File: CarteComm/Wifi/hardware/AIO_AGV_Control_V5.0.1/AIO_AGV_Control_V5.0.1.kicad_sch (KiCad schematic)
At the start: 57 parts, among them J1 DB25_Pins, J2 DB25_Socket, T1 IRF520, T10 IRF520, T11 IRF520, T12 IRF520, T14 IRF520, T15 IRF520, T16 IRF520, T17 IRF520, T18 IRF520, T19 IRF520, T2 IRF520, T20 IRF520, T21 IRF520, T22 IRF520, T23 IRF520, T24 IRF520, T3 IRF520, T4 IRF520, T5 IRF520, T6 IRF520, T7 IRF520, T8 IRF520, T9 IRF520, U1 ESP32-DEVKITC

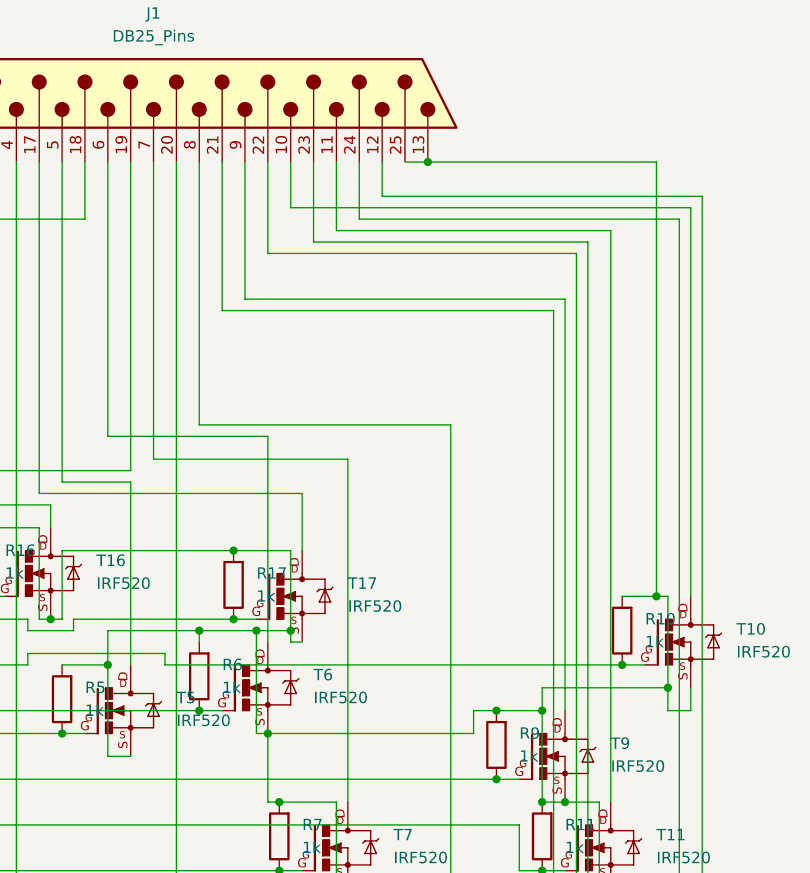
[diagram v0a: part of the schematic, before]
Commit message: test(lora): essais radio d'émission et de réception, côté ESP32 et côté Linux
Deux sous-dossiers dans LoRa/test/, chacun avec un essai d'émission et un de
réception, donc quatre combinaisons possibles. Les deux croisées - ESP32 vers
Linux et Linux vers ESP32 - sont les seules qui prouvent quelque chose : une
implémentation confrontée à elle-même ne démontre que sa propre cohérence.

Le point de conception est là. Une radio qui porte et des trames qui divergent
d'un bit donnent un banc parfait et une panne en atelier, alors les deux côtés
parlent la trame applicative du projet, pas un message d'essai. Côté ESP32 les
sketches compilent le pilote Sx1276Radio et le DutyCycleBudget du dépôt ; côté
Linux, agv_frame.py est un portage fidèle de frame.cpp.

Ce portage n'est pas pris sur parole : test_interop_trame.py compile le codec
C++ du coeur, lui fait produire des vecteurs et compare octet à octet. Six
vecteurs, extension d'horodatage comprise, zéro écart. C'est le seul essai du
dossier qui tourne sans matériel.

Le budget de rapport cyclique est appliqué des deux côtés, accusés compris - un
récepteur qui acquitte est un émetteur. Les deux essais de réception alertent
sous -115 dBm de RSSI : un lien qui passe tout juste ne passe pas une fois un
chariot chargé entre les antennes.

Le brochage ESP32 par défaut reprend les broches relevées libres au KiCad, avec
un static_assert contre IO16 et IO17 qui portent la liaison vers le MEGA.

Le README rappelle qu'un Gate G100 ne peut pas faire tourner les scripts unipi :
boîtier fermé, ni SPI ni GPIO.

Co-Authored-By: Claude Opus 5 <noreply@anthropic.com>
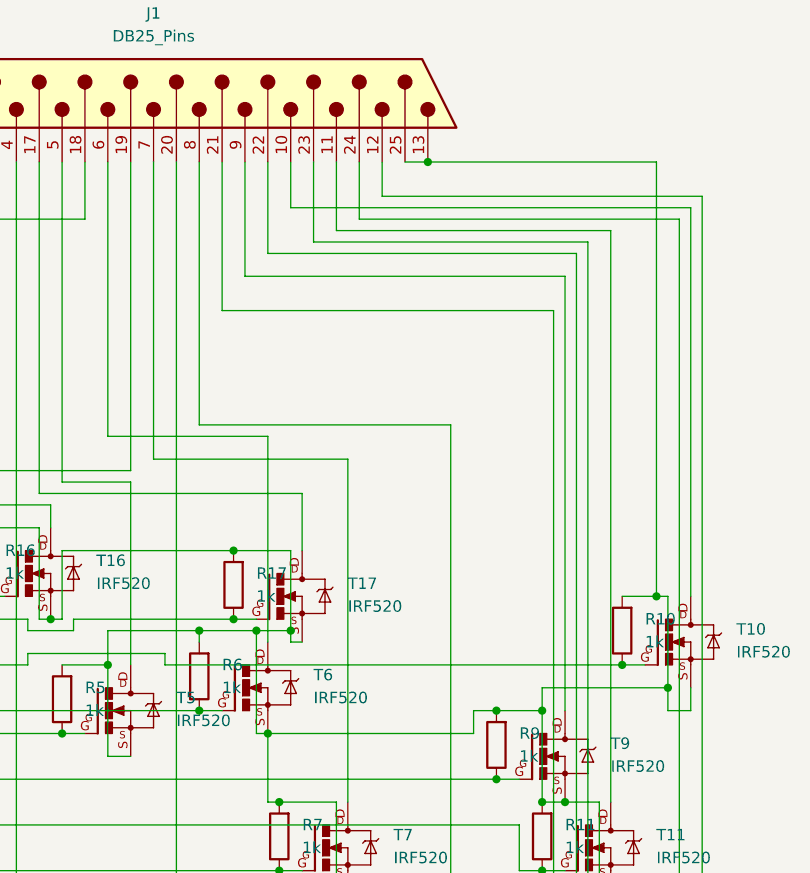
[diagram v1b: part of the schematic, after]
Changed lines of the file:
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@@
-	(wire
-		(pts
-			(xy 266.7 43.18) (xy 266.7 88.9)
-		)
-		(stroke
-			(width 0)
-			(type default)
-		)
-	)
 	(wire
 		(pts
@@
 	(wire
 		(pts
-			(xy 231.14 27.94) (xy 231.14 43.18)
+			(xy 231.14 27.94) (xy 231.14 40.64)
 		)
 		(stroke
@@
 	(wire
 		(pts
-			(xy 231.14 43.18) (xy 266.7 43.18)
+			(xy 231.14 40.64) (xy 266.7 40.64)
 		)
 		(stroke
@@
 		)
 		(stroke
+			(width 0)
+			(type default)
+		)
+	)
+	(wire
+		(pts
+			(xy 266.7 40.64) (xy 266.7 88.9)
+		)
+		(stroke
